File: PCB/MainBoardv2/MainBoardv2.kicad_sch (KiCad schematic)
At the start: 67 parts, among them J1 Conn_02x03_Odd_Even, J10 Conn_01x04_Socket, J2 USB_B_Micro, J3 Conn_02x03_Odd_Even, J4 Conn_01x05_Pin, J5 Conn_01x03_Socket, J6 Screw_Terminal_01x02, J7 Conn_01x04_Socket, J8 Screw_Terminal_01x02, J9 Conn_01x04_Socket, SW1 SW_Push, SW2 Toggle, U1 AZ1117-3.3, U2 STM32F103C8T6TR, U3 SN74HCS4075PWR, U4 TPS56637RPA, Y1 8MHz Crystal

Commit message: pushing progress on mainboard v2 layout
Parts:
- J6, J8: footprint CustomFootprints:1985195 -> CustomFootprints:PHOENIX_1017521
- SW1: footprint Button_Switch_SMD:SW_SPST_B3S-1000 -> Button_Switch_THT:SW_PUSH_6mm_H7.3mm
- renumbered Cboot to Cboot1, Cff to Cff1, Cin to Cin1, Cinx to Cinx1, Cout to Cout1, Rfbb to Rfbb1, Rfbt to Rfbt1, Rff to Rff1, Rpg to Rpg1, TP9 to TP10, TP10 to TP11, TP14 to TP8, TP8 to TP9
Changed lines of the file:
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@@
 		(on_board yes)
 		(dnp no)
-		(property "Reference" "TP10"
+		(property "Reference" "TP11"
 			(at 168.402 178.562 0)
 			(effects
@@
 			(project "MainBoardv2"
 				(path "/d9c43b87-8960-41bd-bfcc-9c305bab2f72"
-					(reference "TP10")
+					(reference "TP11")
 					(unit 1)
 				)
@@
 		(dnp no)
 		(fields_autoplaced yes)
-		(property "Reference" "Cboot"
+		(property "Reference" "Cboot1"
 			(at 72.39 152.4 90)
 			(effects
@@
 			(project "MainBoardv2"
 				(path "/d9c43b87-8960-41bd-bfcc-9c305bab2f72"
-					(reference "Cboot")
+					(reference "Cboot1")
 					(unit 1)
 				)
@@
 			)
 		)
-		(property "Footprint" "CustomFootprints:1985195"
+		(property "Footprint" "CustomFootprints:PHOENIX_1017521"
 			(at 213.36 154.94 0)
 			(effects
@@
 		(on_board yes)
 		(dnp no)
-		(property "Reference" "TP14"
+		(property "Reference" "TP8"
 			(at 215.392 144.526 0)
 			(effects
@@
 			(project "MainBoardv2"
 				(path "/d9c43b87-8960-41bd-bfcc-9c305bab2f72"
-					(reference "TP14")
+					(reference "TP8")
 					(unit 1)
 				)
@@
 		(on_board yes)
 		(dnp no)
-		(property "Reference" "Rfbb"
+		(property "Reference" "Rfbb1"
 			(at 113.03 184.15 90)
 			(effects
@@
 			(project "MainBoardv2"
 				(path "/d9c43b87-8960-41bd-bfcc-9c305bab2f72"
-					(reference "Rfbb")
+					(reference "Rfbb1")
 					(unit 1)
 				)
@@
 		(on_board yes)
 		(dnp no)
-		(property "Reference" "Rff"
+		(property "Reference" "Rff1"
 			(at 102.87 165.1 90)
 			(effects
@@
 			(project "MainBoardv2"
 				(path "/d9c43b87-8960-41bd-bfcc-9c305bab2f72"
-					(reference "Rff")
+					(reference "Rff1")
 					(unit 1)
 				)
@@
 	)
 	(symbol
+		(lib_id "Switch:SW_Push")
+		(at 160.02 86.36 90)
+		(unit 1)
+		(exclude_from_sim no)
+		(in_bom yes)
+		(on_board yes)
+		(dnp no)
+		(fields_autoplaced yes)
+		(property "Reference" "SW1"
+			(at 161.29 85.0899 90)
+			(effects
+				(font
+					(size 1.27 1.27)
+				)
+				(justify right)
+			)
+		)
+		(property "Value" "SW_Push"
+			(at 161.29 87.6299 90)
+			(effects
+				(font
+					(size 1.27 1.27)
+				)
+				(justify right)
+			)
+		)
+		(property "Footprint" "Button_Switch_THT:SW_PUSH_6mm_H7.3mm"
+			(at 154.94 86.36 0)
+			(effects
+				(font
+					(size 1.27 1.27)
+				)
+				(hide yes)
+			)
+		)
+		(property "Datasheet" "~"
+			(at 154.94 86.36 0)
+			(effects
+				(font
+					(size 1.27 1.27)
+				)
+				(hide yes)
+			)
+		)
+		(property "Description" "Push button switch, generic, two pins"
+			(at 160.02 86.36 0)
+			(effects
+				(font
+					(size 1.27 1.27)
+				)
+				(hide yes)
+			)
+		)
+		(pin "1"
+		)
+		(pin "2"
+		)
+		(instances
+			(project "MainBoardv2"
+				(path "/d9c43b87-8960-41bd-bfcc-9c305bab2f72"
+					(reference "SW1")
+					(unit 1)
+				)
+			)
+		)
+	)
+	(symbol
 		(lib_name "GND_3")
 		(lib_id "power:GND")
@@
 		(on_board yes)
 		(dnp no)
-		(property "Reference" "Cff"
+		(property "Reference" "Cff1"
 			(at 95.758 170.18 0)
 			(effects
@@
 			(project "MainBoardv2"
 				(path "/d9c43b87-8960-41bd-bfcc-9c305bab2f72"
-					(reference "Cff")
+					(reference "Cff1")
 					(unit 1)
 				)
@@
 		(on_board yes)
 		(dnp no)
-		(property "Reference" "Rfbt"
+		(property "Reference" "Rfbt1"
 			(at 113.03 171.45 90)
 			(effects
@@
 			(project "MainBoardv2"
 				(path "/d9c43b87-8960-41bd-bfcc-9c305bab2f72"
-					(reference "Rfbt")
+					(reference "Rfbt1")
 					(unit 1)
 				)
@@
 		(on_board yes)
 		(dnp no)
-		(property "Reference" "TP9"
+		(property "Reference" "TP10"
 			(at 168.402 162.052 0)
 			(effects
@@
 			(project "MainBoardv2"
 				(path "/d9c43b87-8960-41bd-bfcc-9c305bab2f72"
-					(reference "TP9")
+					(reference "TP10")
 					(unit 1)
 				)
@@
 		(on_board yes)
 		(dnp no)
-		(property "Reference" "Rpg"
+		(property "Reference" "Rpg1"
 			(at 76.2 170.18 90)
 			(effects
@@
 			(project "MainBoardv2"
 				(path "/d9c43b87-8960-41bd-bfcc-9c305bab2f72"
-					(reference "Rpg")
+					(reference "Rpg1")
 					(unit 1)
 				)
@@
 		(on_board yes)
 		(dnp no)
-		(property "Reference" "TP8"
+		(property "Reference" "TP9"
 			(at 26.162 152.908 0)
 			(effects
@@
 			(project "MainBoardv2"
 				(path "/d9c43b87-8960-41bd-bfcc-9c305bab2f72"
-					(reference "TP8")
+					(reference "TP9")
 					(unit 1)
 				)
@@
 		(on_board yes)
 		(dnp no)
-		(property "Reference" "Cout"
+		(property "Reference" "Cout1"
 			(at 125.222 172.72 0)
 			(effects
@@
 			(project "MainBoardv2"
 				(path "/d9c43b87-8960-41bd-bfcc-9c305bab2f72"
-					(reference "Cout")
+					(reference "Cout1")
 					(unit 1)
 				)
@@
 	)
 	(symbol
-		(lib_id "Switch:SW_Push")
-		(at 160.02 86.36 90)
-		(unit 1)
-		(exclude_from_sim no)
-		(in_bom yes)
-		(on_board yes)
-		(dnp no)
-		(fields_autoplaced yes)
-		(property "Reference" "SW1"
-			(at 161.163 85.5253 90)
-			(effects
-				(font
-					(size 1.27 1.27)
-				)
-				(justify right)
-			)
-		)
-		(property "Value" "SW_Push"
-			(at 161.163 88.0622 90)
-			(effects
-				(font
-					(size 1.27 1.27)
-				)
-				(justify right)
-			)
-		)
-		(property "Footprint" "Button_Switch_SMD:SW_SPST_B3S-1000"
-			(at 154.94 86.36 0)
-			(effects
-				(font
-					(size 1.27 1.27)
-				)
-				(hide yes)
-			)
-		)
-		(property "Datasheet" "https://www.digikey.com/en/products/detail/omron-electronics-inc-emc-div/B3S-1000/20686"
-			(at 154.94 86.36 0)
-			(effects
-				(font
-					(size 1.27 1.27)
-				)
-				(hide yes)
-			)
-		)
-		(property "Description" ""
-			(at 160.02 86.36 0)
-			(effects
-				(font
-					(size 1.27 1.27)
-				)
-				(hide yes)
-			)
-		)
-		(pin "1"
-		)
-		(pin "2"
-		)
-		(instances
-			(project "MainBoardv2"
-				(path "/d9c43b87-8960-41bd-bfcc-9c305bab2f72"
-					(reference "SW1")
-					(unit 1)
-				)
-			)
-		)
-	)
-	(symbol
 		(lib_id "basic:R")
 		(at 133.35 52.07 0)
@@
 		(on_board yes)
 		(dnp no)
-		(property "Reference" "Cin"
+		(property "Reference" "Cin1"
 			(at 20.066 172.72 0)
 			(effects
@@
 			(project "MainBoardv2"
 				(path "/d9c43b87-8960-41bd-bfcc-9c305bab2f72"
-					(reference "Cin")
+					(reference "Cin1")
 					(unit 1)
 				)
@@
 		(on_board yes)
 		(dnp no)
-		(property "Reference" "Cinx"
+		(property "Reference" "Cinx1"
 			(at 32.258 172.72 0)
 			(effects
@@
 			(project "MainBoardv2"
 				(path "/d9c43b87-8960-41bd-bfcc-9c305bab2f72"
-					(reference "Cinx")
+					(reference "Cinx1")
 					(unit 1)
 				)
@@
 			)
 		)
-		(property "Footprint" "CustomFootprints:1985195"
+		(property "Footprint" "CustomFootprints:PHOENIX_1017521"
 			(at 269.24 158.75 0)
 			(effects

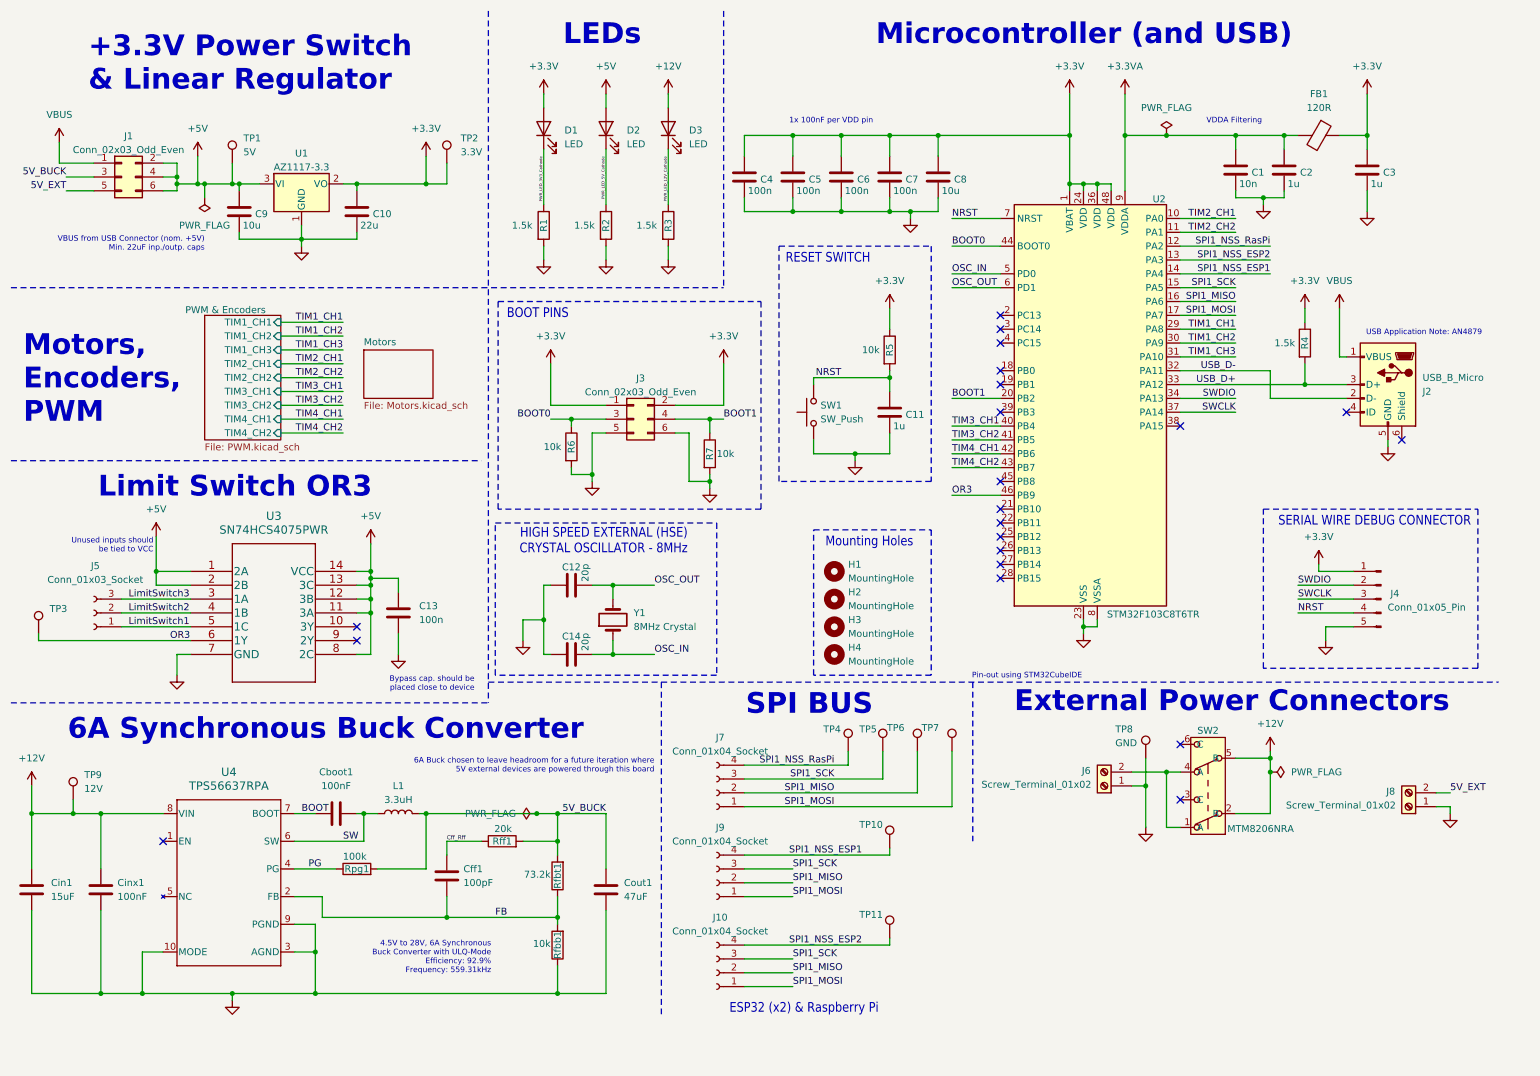
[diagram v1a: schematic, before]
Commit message: Main Board v2 Rough component layout complete
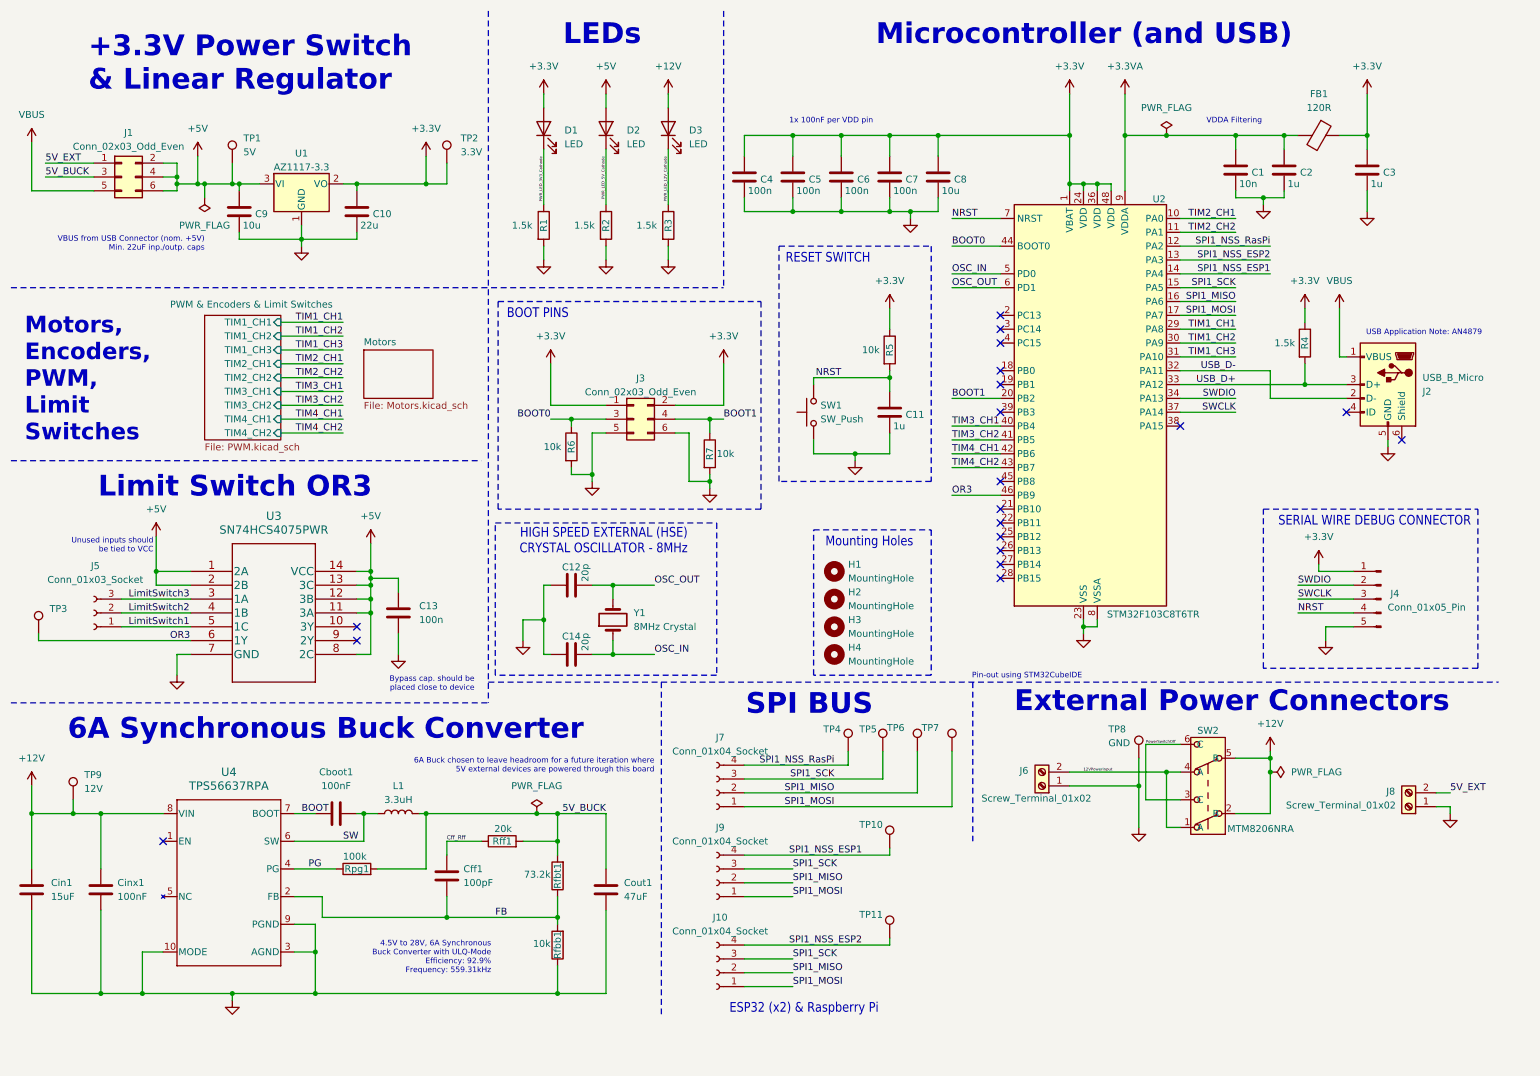
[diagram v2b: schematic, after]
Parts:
- J1, J3: footprint Connector_PinSocket_2.54mm:PinSocket_2x03_P2.54mm_Vertical -> Connector_PinHeader_2.54mm:PinHeader_2x03_P2.54mm_Vertical
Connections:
- net 5V_EXT: now also J1.1 (Pin_1); no longer J1.5 (Pin_5)
- net VBUS: now also J1.5 (Pin_5); no longer J1.1 (Pin_1)
- net 12VPowerInput: now reaches J6.2 (Pin_2), SW2.1 (A), SW2.4 (A)
- net PowerSwitchOff: now reaches SW2.3 (C)
- net PowerSwitchOff: now also SW2.6 (C)
- no-connect marks 21 -> 19
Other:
- sheet PWM & Encoders renamed PWM & Encoders & Limit Switches
- note added: "Motors, Encoders, PWM, Limit Switches"
- note removed: "Motors, Encoders, PWM"
- moved on the sheet: J6, TP8

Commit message: updating layout progress, adding limit switch extra circuitry
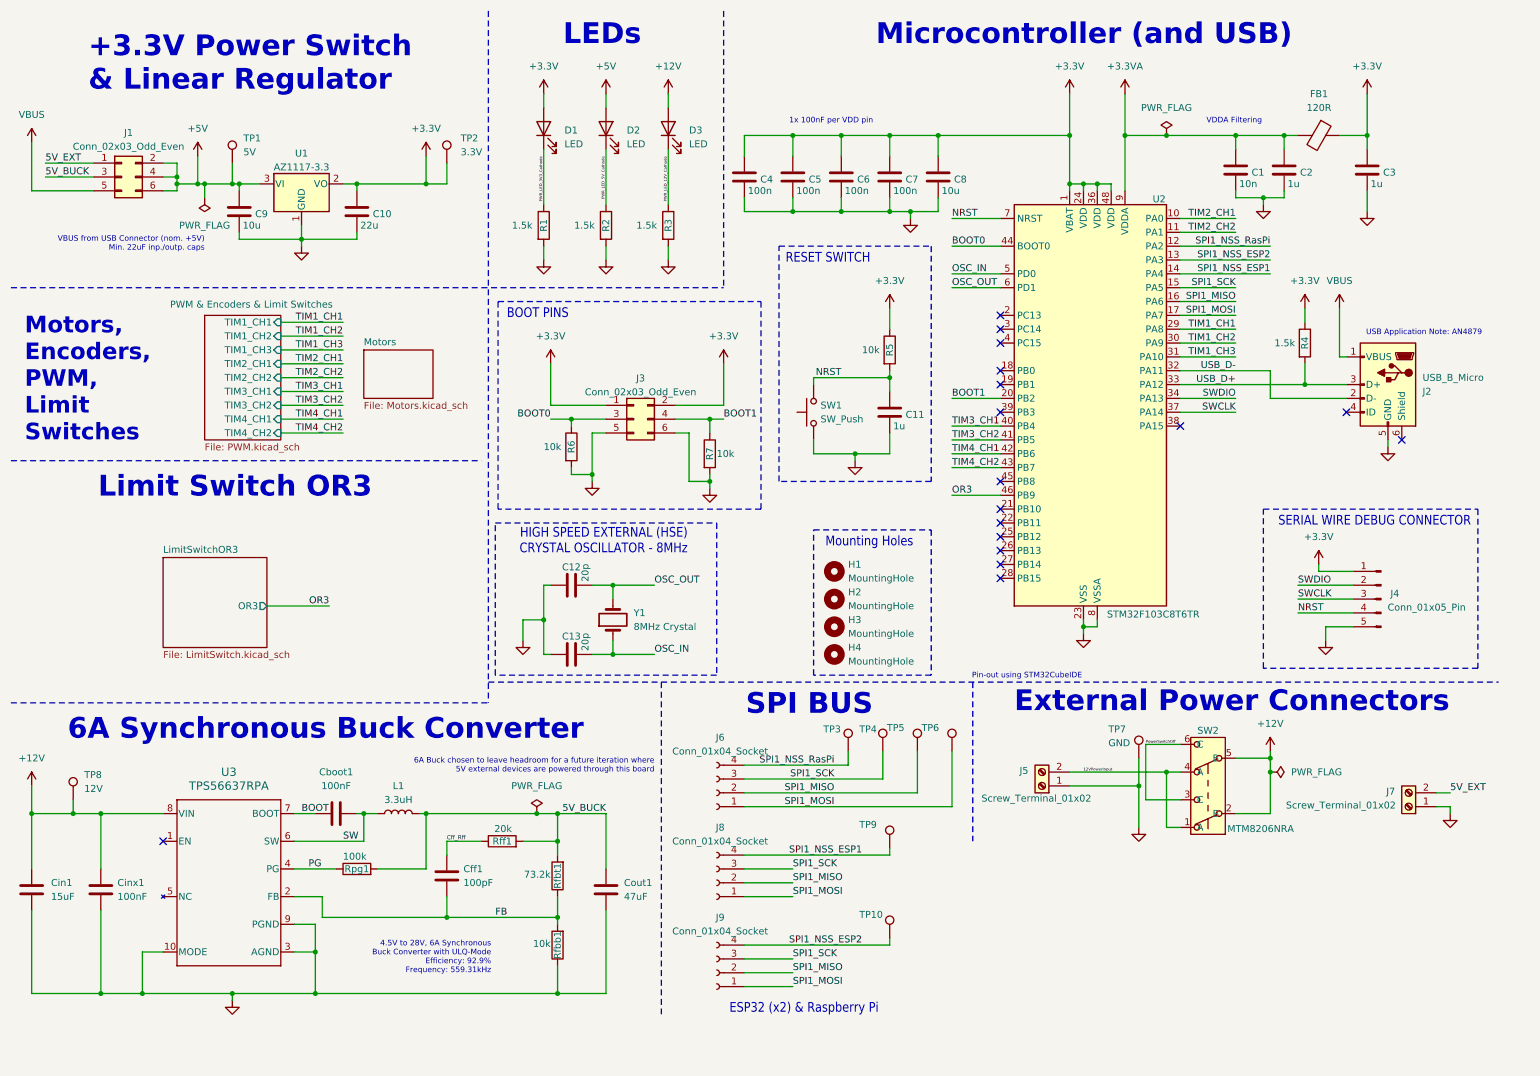
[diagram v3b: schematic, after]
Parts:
- removed C13: 100n, Capacitor_SMD:C_0603_1608Metric, symbol Device:C
- removed J5: Conn_01x03_Socket, Connector_PinHeader_2.54mm:PinHeader_1x03_P2.54mm_Vertical, symbol Connector:Conn_01x03_Socket
- removed TP3: White, TestPoint:TestPoint_Keystone_5000-5004_Miniature, symbol Connector:TestPoint
- removed U3: SN74HCS4075PWR, CustomFootprints:SN74HCS4075PWR, symbol CustomSymbols:SN74HCS4075PWR
- J6: renamed from J7; footprint Connector_PinHeader_2.54mm:PinHeader_1x04_P2.54mm_Vertical -> Connector_PinHeader_2.54mm:PinHeader_1x04_P2.54mm_Horizontal
- J8: renamed from J9; footprint Connector_PinHeader_2.54mm:PinHeader_1x04_P2.54mm_Vertical -> Connector_PinHeader_2.54mm:PinHeader_1x04_P2.54mm_Horizontal
- J9: renamed from J10; footprint Connector_PinHeader_2.54mm:PinHeader_1x04_P2.54mm_Vertical -> Connector_PinHeader_2.54mm:PinHeader_1x04_P2.54mm_Horizontal
- renumbered C14 to C13, J6 to J5, J8 to J7, TP11 to TP10, TP4 to TP3, TP5 to TP4, TP6 to TP5, TP7 to TP6, TP8 to TP7, TP9 to TP8, TP10 to TP9, U4 to U3
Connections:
- no-connect marks 19 -> 17
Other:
- added sheet LimitSwitchOR3 (LimitSwitch.kicad_sch)
- note removed: "Bypass cap. should be placed close to device"
- note removed: "Unused inputs should be tied to VCC"
